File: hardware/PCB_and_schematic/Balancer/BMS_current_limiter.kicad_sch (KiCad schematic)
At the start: 38 parts, among them J1 BATT, J12 External Current Shunt, J2 OUT, Q1 BC817, Q2 BC337, Q3 BC327, Q4 PMOS, Q5 PMOS, Q6 BC337, Q7 BC327, Q8 BC817

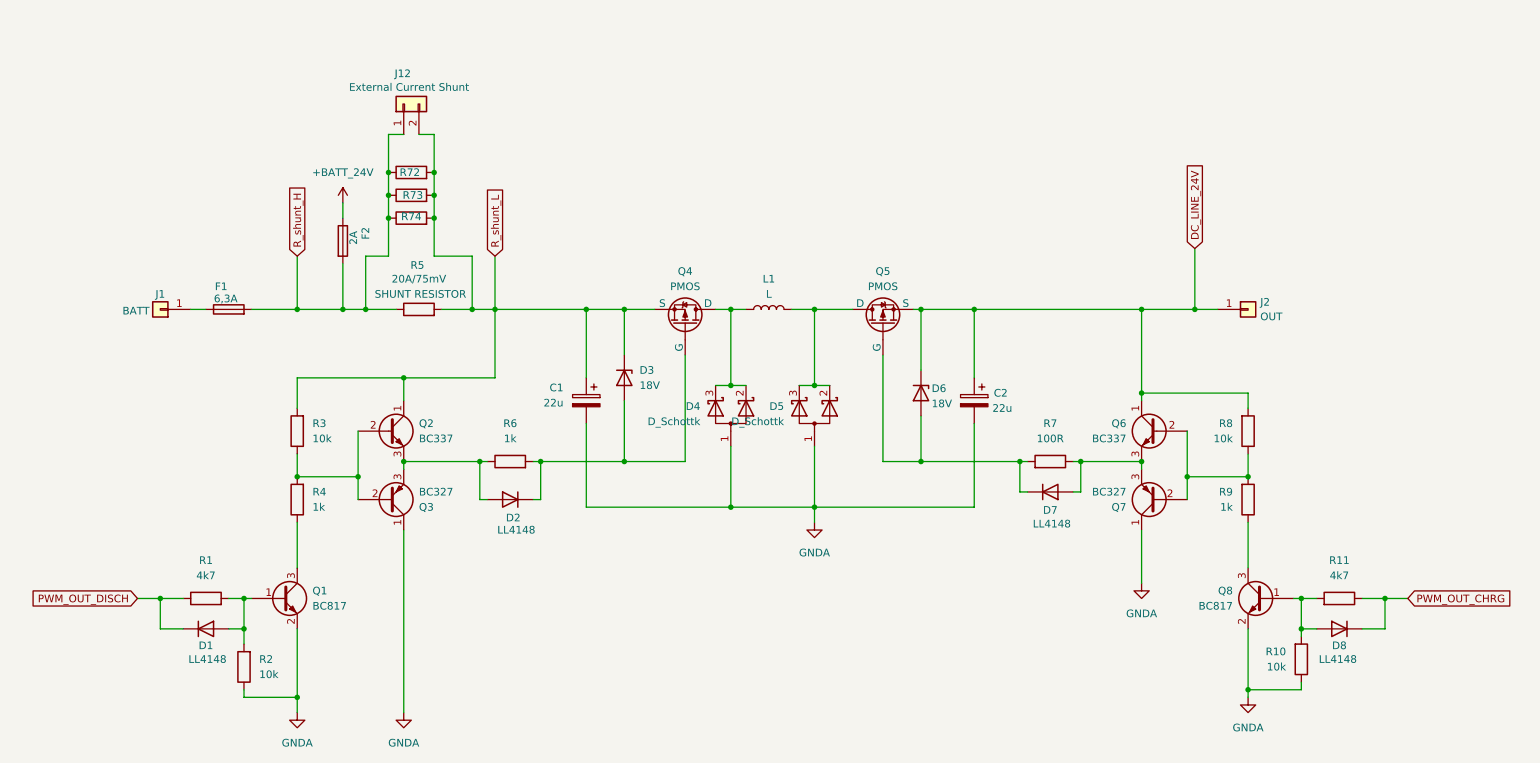
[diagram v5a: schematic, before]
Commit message: balancer pcb progress
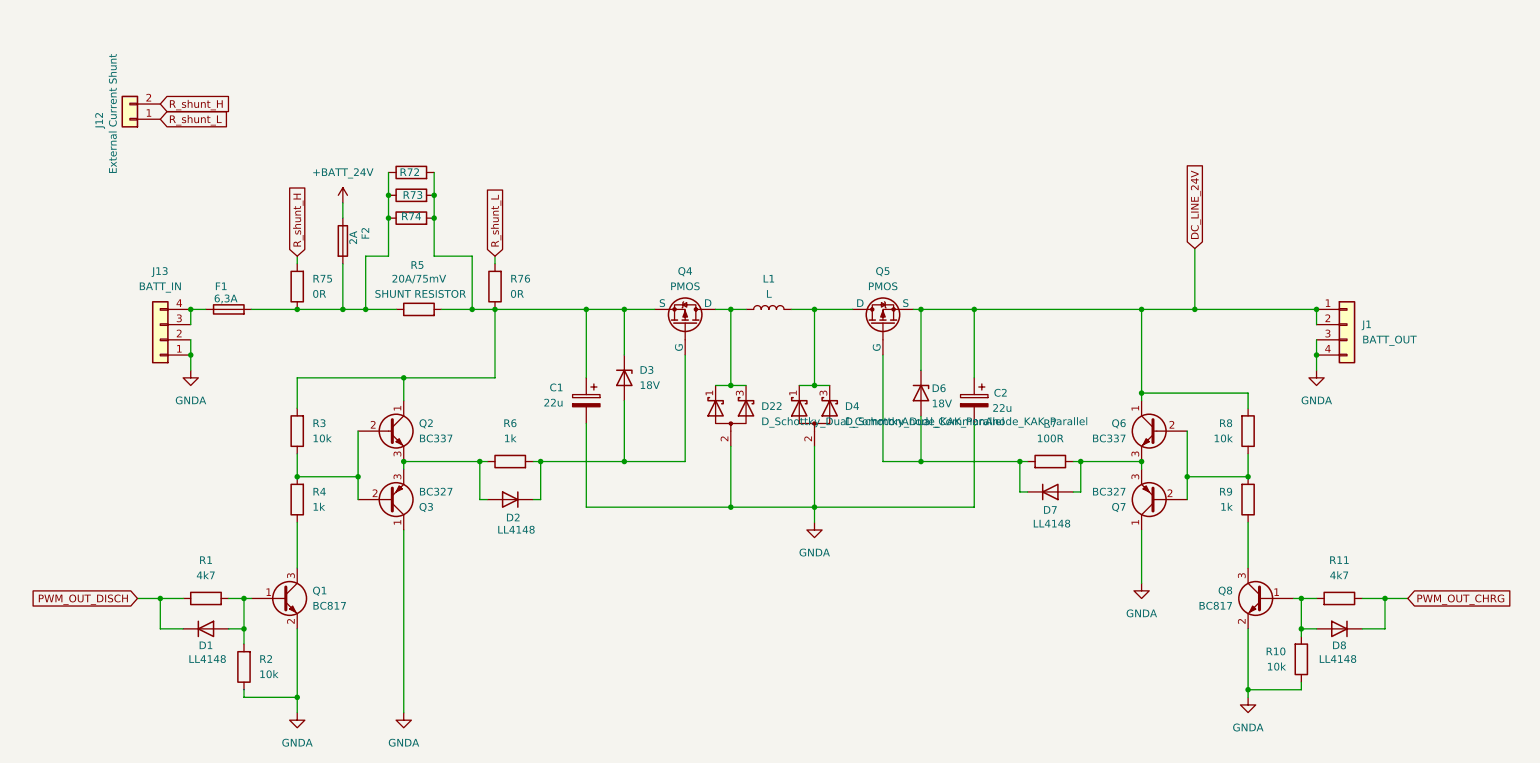
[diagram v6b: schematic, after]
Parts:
- removed D4, D5: D_Schottk, My-Footprints:TO-220-3_V_Thick_Pads, symbol Device:D_Schottky_Dual_CommonAnode_AKK_Parallel
- removed J1: BATT, Connector_Pin:Pin_D1.4mm_L8.5mm_W2.8mm_FlatFork, symbol Connector_Generic:Conn_01x01
- removed J2: OUT, Connector_Pin:Pin_D1.4mm_L8.5mm_W2.8mm_FlatFork, symbol Connector_Generic:Conn_01x01
- added D22, D4: D_Schottky_Dual_CommonAnode_KAK_Parallel, My-Footprints:TO-220-3_V_Thick_Pads, symbol Device:D_Schottky_Dual_CommonAnode_KAK_Parallel
- added J1: BATT_OUT, My-Footprints-connectors:Flat-6,3mm-connector-4P, symbol Connector_Generic:Conn_01x04
- added J13: BATT_IN, My-Footprints-connectors:Flat-6,3mm-connector-4P, symbol Connector_Generic:Conn_01x04
- added R75, R76: 0R, Resistor_SMD:R_0805_2012Metric, symbol Device:R
- F1: footprint Fuse:Fuse_Blade_ATO_directSolder -> My-Footprints:Fuse_Blade_ATO_directSolder
- F2: footprint Fuse:Fuse_Blade_ATO_directSolder -> My-Footprints:Fuseholder_Clip-5x20mm_Eaton_1A5601-01_Inline_P20.80x6.76mm_D1.70mm_Horizontal
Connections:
- net DC_LINE_24V: now also J1.1 (Pin_1), J1.2 (Pin_2)
- net GNDA: now also D22.2 (A), D4.2 (A), J1.3 (Pin_3), J1.4 (Pin_4), J13.1 (Pin_1), J13.2 (Pin_2)
- net R_shunt_H: now also J12.2 (Pin_2), R75.2; no longer F1.2, F2.2, J12.1 (Pin_1), R5.1, R72.1, R73.1, R74.1
- net R_shunt_L: now also J12.1 (Pin_1), R76.2; no longer C1.1, D3.1 (K), J12.2 (Pin_2), Q2.1 (C), Q4.3 (S), R3.2, R5.2, R72.2, R73.2, R74.2
- net at L1.1, Q4.1 (D): now also D22.1 (K), D22.3 (K)
- net at L1.2, Q5.1 (D): now also D4.1 (K), D4.3 (K)
- net at F1.1: now also J13.3 (Pin_3), J13.4 (Pin_4)
- new net: C1.1, D3.1 (K), Q2.1 (C), Q4.3 (S), R3.2, R5.2, R72.2, R73.2, R74.2, R76.1
- new net: F1.2, F2.2, R5.1, R72.1, R73.1, R74.1, R75.1
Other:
- moved on the sheet: J12

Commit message: Balancer routing
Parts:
- C1, C2: footprint Capacitor_Tantalum_SMD:CP_EIA-3528-21_Kemet-B -> Capacitor_SMD:CP_Elec_6.3x4.9
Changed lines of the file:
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@@
 			)
 		)
-		(property "Footprint" "Capacitor_Tantalum_SMD:CP_EIA-3528-21_Kemet-B"
+		(property "Footprint" "Capacitor_SMD:CP_Elec_6.3x4.9"
 			(at 124.7648 76.2 0)
 			(effects
@@
 			)
 		)
-		(property "Footprint" "Capacitor_Tantalum_SMD:CP_EIA-3528-21_Kemet-B"
+		(property "Footprint" "Capacitor_SMD:CP_Elec_6.3x4.9"
 			(at 189.5348 76.2 0)
 			(effects

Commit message: PCB footprint changes
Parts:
- C1, C2: value 22u -> 100u/35V; footprint Capacitor_SMD:CP_Elec_6.3x4.9 -> Capacitor_THT:CP_Radial_D8.0mm_P3.50mm
- R74: value R -> 20A/75mV
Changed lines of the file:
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@@
 	)
 	(junction
-		(at 100.33 41.91)
-		(diameter 0)
-		(color 0 0 0 0)
-	)
-	(junction
 		(at 106.68 57.15)
 		(diameter 0)
@@
 	)
 	(junction
-		(at 92.71 41.91)
-		(diameter 0)
-		(color 0 0 0 0)
-	)
-	(junction
 		(at 92.71 38.1)
 		(diameter 0)
@@
 	)
 	(junction
+		(at 100.33 41.91)
+		(diameter 0)
+		(color 0 0 0 0)
+	)
+	(junction
 		(at 247.65 64.77)
 		(diameter 0)
@@
 		(color 0 0 0 0)
 	)
+	(junction
+		(at 92.71 41.91)
+		(diameter 0)
+		(color 0 0 0 0)
+	)
 	(wire
 		(pts
@@
 	(wire
 		(pts
-			(xy 92.71 48.26) (xy 92.71 41.91)
-		)
-		(stroke
-			(width 0)
-			(type default)
-		)
-	)
-	(wire
-		(pts
 			(xy 125.73 90.17) (xy 125.73 76.2)
 		)
@@
 	(wire
 		(pts
-			(xy 100.33 48.26) (xy 100.33 41.91)
-		)
-		(stroke
-			(width 0)
-			(type default)
-		)
-	)
-	(wire
-		(pts
 			(xy 54.61 110.49) (xy 54.61 105.41)
 		)
@@
 	(wire
 		(pts
+			(xy 100.33 41.91) (xy 100.33 48.26)
+		)
+		(stroke
+			(width 0)
+			(type default)
+		)
+	)
+	(wire
+		(pts
 			(xy 66.04 105.41) (xy 68.58 105.41)
 		)
@@
 	(wire
 		(pts
+			(xy 92.71 41.91) (xy 92.71 48.26)
+		)
+		(stroke
+			(width 0)
+			(type default)
+		)
+	)
+	(wire
+		(pts
 			(xy 92.71 38.1) (xy 92.71 41.91)
 		)
@@
 	(symbol
 		(lib_id "Device:R")
+		(at 96.52 41.91 90)
+		(unit 1)
+		(exclude_from_sim no)
+		(in_bom yes)
+		(on_board yes)
+		(dnp no)
+		(property "Reference" "R74"
+			(at 96.774 41.91 90)
+			(effects
+				(font
+					(size 1.27 1.27)
+				)
+			)
+		)
+		(property "Value" "20A/75mV"
+			(at 96.52 36.83 90)
+			(effects
+				(font
+					(size 1.27 1.27)
+				)
+				(hide yes)
+			)
+		)
+		(property "Footprint" "Resistor_THT:R_Axial_DIN0309_L9.0mm_D3.2mm_P20.32mm_Horizontal"
+			(at 96.52 43.688 90)
+			(effects
+				(font
+					(size 1.27 1.27)
+				)
+				(hide yes)
+			)
+		)
+		(property "Datasheet" "~"
+			(at 96.52 41.91 0)
+			(effects
+				(font
+					(size 1.27 1.27)
+				)
+				(hide yes)
+			)
+		)
+		(property "Description" "SHUNT RESISTOR"
+			(at 96.774 39.37 90)
+			(effects
+				(font
+					(size 1.27 1.27)
+				)
+				(hide yes)
+			)
+		)
+		(property "Field5" ""
+			(at 96.52 41.91 90)
+			(effects
+				(font
+					(size 1.27 1.27)
+				)
+				(hide yes)
+			)
+		)
+		(pin "1"
+		)
+		(pin "2"
+		)
+		(instances
+			(project "Balancer"
+				(path "/555ba40f-9abb-4b99-82c6-07e888fda9fd/f65ef685-3e95-4f8a-97fe-0688761539e6"
+					(reference "R74")
+					(unit 1)
+				)
+			)
+		)
+	)
+	(symbol
+		(lib_id "Device:R")
 		(at 77.47 88.9 180)
 		(unit 1)
@@
 			)
 		)
-		(property "Value" "22u"
+		(property "Value" "100u/35V"
 			(at 121.92 72.7709 0)
 			(effects
@@
 			)
 		)
-		(property "Footprint" "Capacitor_SMD:CP_Elec_6.3x4.9"
+		(property "Footprint" "Capacitor_THT:CP_Radial_D8.0mm_P3.50mm"
 			(at 124.7648 76.2 0)
 			(effects
@@
 			)
 		)
-		(property "Value" "22u"
-			(at 196.85 73.66 0)
+		(property "Value" "100u/35V"
+			(at 203.2 73.406 0)
 			(effects
 				(font
@@
 			)
 		)
-		(property "Footprint" "Capacitor_SMD:CP_Elec_6.3x4.9"
+		(property "Footprint" "Capacitor_THT:CP_Radial_D8.0mm_P3.50mm"
 			(at 189.5348 76.2 0)
 			(effects
@@
 					(unit 1)
 				)
-			)
-		)
-	)
-	(symbol
-		(lib_id "Device:R")
-		(at 96.52 41.91 90)
-		(unit 1)
-		(exclude_from_sim no)
-		(in_bom yes)
-		(on_board yes)
-		(dnp no)
-		(property "Reference" "R74"
-			(at 96.52 41.656 90)
-			(effects
-				(font
-					(size 1.27 1.27)
-				)
-			)
-		)
-		(property "Value" "R"
-			(at 96.52 41.91 90)
-			(effects
-				(font
-					(size 1.27 1.27)
-				)
-				(hide yes)
-			)
-		)
-		(property "Footprint" "Resistor_THT:R_Axial_DIN0309_L9.0mm_D3.2mm_P20.32mm_Horizontal"
-			(at 96.52 43.688 90)
-			(effects
-				(font
-					(size 1.27 1.27)
-				)
-				(hide yes)
-			)
-		)
-		(property "Datasheet" "~"
-			(at 96.52 41.91 0)
-			(effects
-				(font
-					(size 1.27 1.27)
-				)
-				(hide yes)
-			)
-		)
-		(property "Description" "SHUNT RESISTOR"
-			(at 96.774 39.37 90)
-			(effects
-				(font
-					(size 1.27 1.27)
-				)
-				(hide yes)
-			)
-		)
-		(property "Field5" ""
-			(at 96.52 41.91 90)
-			(effects
-				(font
-					(size 1.27 1.27)
-				)
-				(hide yes)
-			)
-		)
-		(pin "1"
-		)
-		(pin "2"
-		)
-		(instances
-			(project "Balancer"
-				(path "/555ba40f-9abb-4b99-82c6-07e888fda9fd/f65ef685-3e95-4f8a-97fe-0688761539e6"
-					(reference "R74")
-					(unit 1)
-				)
